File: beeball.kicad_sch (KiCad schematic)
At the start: 13 parts, among them SW1 SW_Push, SW2 SW_Push, SW3 SW_Push, U1 SeeeduinoXIAO, U2 PMW3360DM-T2QU, U3 TLV70019_SOT23-5

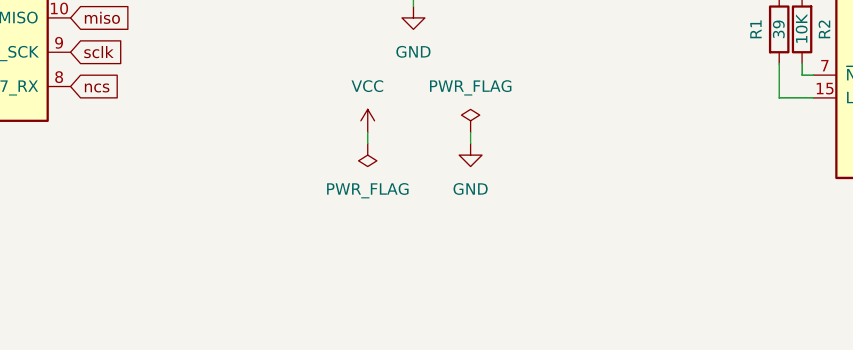
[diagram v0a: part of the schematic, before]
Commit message: Fix battery cutout, change M2 mounting holes to M3, change Choc switch footprint to MX+Choc+Alps footprint
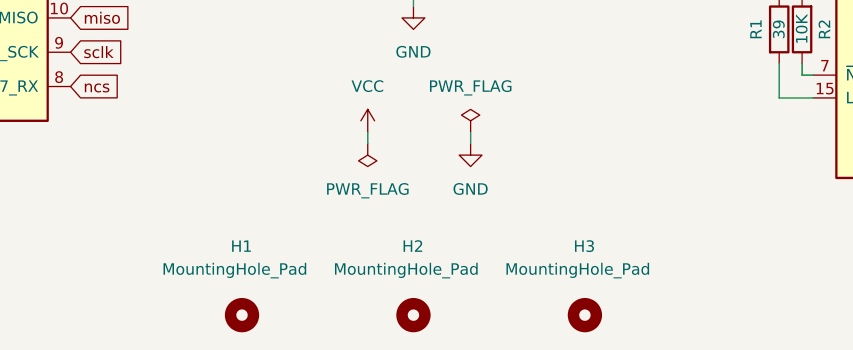
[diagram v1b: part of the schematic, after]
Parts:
- added H1, H2, H3: MountingHole_Pad, MountingHole:MountingHole_3.2mm_M3_Pad, symbol Mechanical:MountingHole
- SW1, SW2, SW3: footprint Project Footprints:Kailh-PG1350-1u -> Project Footprints:MX-Alps-Choc-1U
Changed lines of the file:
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@@
     (pin "1")
+  )
+  (symbol (lib_id "Mechanical:MountingHole") (at 176.53 87.63 0) (unit 1)
+    (in_bom yes) (on_board yes)
+    (property "Reference" "H2" (id 0) (at 175.26 80.01 0)
+      (effects (font (size 1.27 1.27)) (justify left))
+    )
+    (property "Value" "MountingHole_Pad" (id 1) (at 167.64 82.55 0)
+      (effects (font (size 1.27 1.27)) (justify left))
+    )
+    (property "Footprint" "MountingHole:MountingHole_3.2mm_M3_Pad" (id 2) (at 176.53 87.63 0)
+      (effects (font (size 1.27 1.27)) hide)
+    )
+    (property "Datasheet" "~" (id 3) (at 176.53 87.63 0)
+      (effects (font (size 1.27 1.27)) hide)
+    )
   )
   (symbol (lib_id "Device:R") (at 217.17 55.88 0) (unit 1)
@@
     (property "Reference" "SW2" (id 0) (at 52.07 30.861 0))
     (property "Value" "SW_Push" (id 1) (at 52.07 33.1724 0))
-    (property "Footprint" "Project Footprints:Kailh-PG1350-1u" (id 2) (at 52.07 33.02 0)
+    (property "Footprint" "Project Footprints:MX-Alps-Choc-1U" (id 2) (at 52.07 33.02 0)
       (effects (font (size 1.27 1.27)) hide)
     )
@@
     (property "Reference" "SW1" (id 0) (at 35.56 30.861 0))
     (property "Value" "SW_Push" (id 1) (at 35.56 33.1724 0))
-    (property "Footprint" "Project Footprints:Kailh-PG1350-1u" (id 2) (at 35.56 33.02 0)
+    (property "Footprint" "Project Footprints:MX-Alps-Choc-1U" (id 2) (at 35.56 33.02 0)
       (effects (font (size 1.27 1.27)) hide)
     )
@@
     )
     (pin "1")
+  )
+  (symbol (lib_id "Mechanical:MountingHole") (at 157.48 87.63 0) (unit 1)
+    (in_bom yes) (on_board yes)
+    (property "Reference" "H1" (id 0) (at 156.21 80.01 0)
+      (effects (font (size 1.27 1.27)) (justify left))
+    )
+    (property "Value" "MountingHole_Pad" (id 1) (at 148.59 82.55 0)
+      (effects (font (size 1.27 1.27)) (justify left))
+    )
+    (property "Footprint" "MountingHole:MountingHole_3.2mm_M3_Pad" (id 2) (at 157.48 87.63 0)
+      (effects (font (size 1.27 1.27)) hide)
+    )
+    (property "Datasheet" "~" (id 3) (at 157.48 87.63 0)
+      (effects (font (size 1.27 1.27)) hide)
+    )
   )
   (symbol (lib_id "power:GND") (at 40.64 39.37 0) (unit 1)
@@
     )
     (pin "1")
+  )
+  (symbol (lib_id "Mechanical:MountingHole") (at 195.58 87.63 0) (unit 1)
+    (in_bom yes) (on_board yes)
+    (property "Reference" "H3" (id 0) (at 194.31 80.01 0)
+      (effects (font (size 1.27 1.27)) (justify left))
+    )
+    (property "Value" "MountingHole_Pad" (id 1) (at 186.69 82.55 0)
+      (effects (font (size 1.27 1.27)) (justify left))
+    )
+    (property "Footprint" "MountingHole:MountingHole_3.2mm_M3_Pad" (id 2) (at 195.58 87.63 0)
+      (effects (font (size 1.27 1.27)) hide)
+    )
+    (property "Datasheet" "~" (id 3) (at 195.58 87.63 0)
+      (effects (font (size 1.27 1.27)) hide)
+    )
   )
   (symbol (lib_id "Device:C") (at 167.64 46.99 0) (unit 1)
@@
     (property "Reference" "SW3" (id 0) (at 68.58 30.861 0))
     (property "Value" "SW_Push" (id 1) (at 68.58 33.1724 0))
-    (property "Footprint" "Project Footprints:Kailh-PG1350-1u" (id 2) (at 68.58 33.02 0)
+    (property "Footprint" "Project Footprints:MX-Alps-Choc-1U" (id 2) (at 68.58 33.02 0)
       (effects (font (size 1.27 1.27)) hide)
     )
@@
       (reference "C4") (unit 1) (value "0.1uF") (footprint "Capacitor_SMD:C_0805_2012Metric")
     )
+    (path "/6a86cf05-0add-42b9-a9a0-9b4aeb996306"
+      (reference "H1") (unit 1) (value "MountingHole_Pad") (footprint "MountingHole:MountingHole_3.2mm_M3_Pad")
+    )
+    (path "/1291612c-9680-4f68-9209-36d8bcacf249"
+      (reference "H2") (unit 1) (value "MountingHole_Pad") (footprint "MountingHole:MountingHole_3.2mm_M3_Pad")
+    )
+    (path "/74ae0038-0133-4cb9-bb45-74ec7afdfbd3"
+      (reference "H3") (unit 1) (value "MountingHole_Pad") (footprint "MountingHole:MountingHole_3.2mm_M3_Pad")
+    )
     (path "/14ed50ef-bdf0-47cd-8a0b-cfc99af743a0"
       (reference "R1") (unit 1) (value "39") (footprint "Resistor_SMD:R_0805_2012Metric")
@@
     )
     (path "/4aa52e76-8df3-4a0c-b2db-be7ae9ce5fbb"
-      (reference "SW1") (unit 1) (value "SW_Push") (footprint "Project Footprints:Kailh-PG1350-1u")
+      (reference "SW1") (unit 1) (value "SW_Push") (footprint "Project Footprints:MX-Alps-Choc-1U")
     )
     (path "/39bf60a3-fdf8-491d-a06c-055f6b4cb421"
-      (reference "SW2") (unit 1) (value "SW_Push") (footprint "Project Footprints:Kailh-PG1350-1u")
+      (reference "SW2") (unit 1) (value "SW_Push") (footprint "Project Footprints:MX-Alps-Choc-1U")
     )
     (path "/afa9596b-7321-4d8b-bae4-34853e850ba4"
-      (reference "SW3") (unit 1) (value "SW_Push") (footprint "Project Footprints:Kailh-PG1350-1u")
+      (reference "SW3") (unit 1) (value "SW_Push") (footprint "Project Footprints:MX-Alps-Choc-1U")
     )
     (path "/95a936b4-1122-4875-af7e-49f5189decf2"
